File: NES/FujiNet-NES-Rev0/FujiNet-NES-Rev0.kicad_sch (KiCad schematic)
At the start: 0 parts

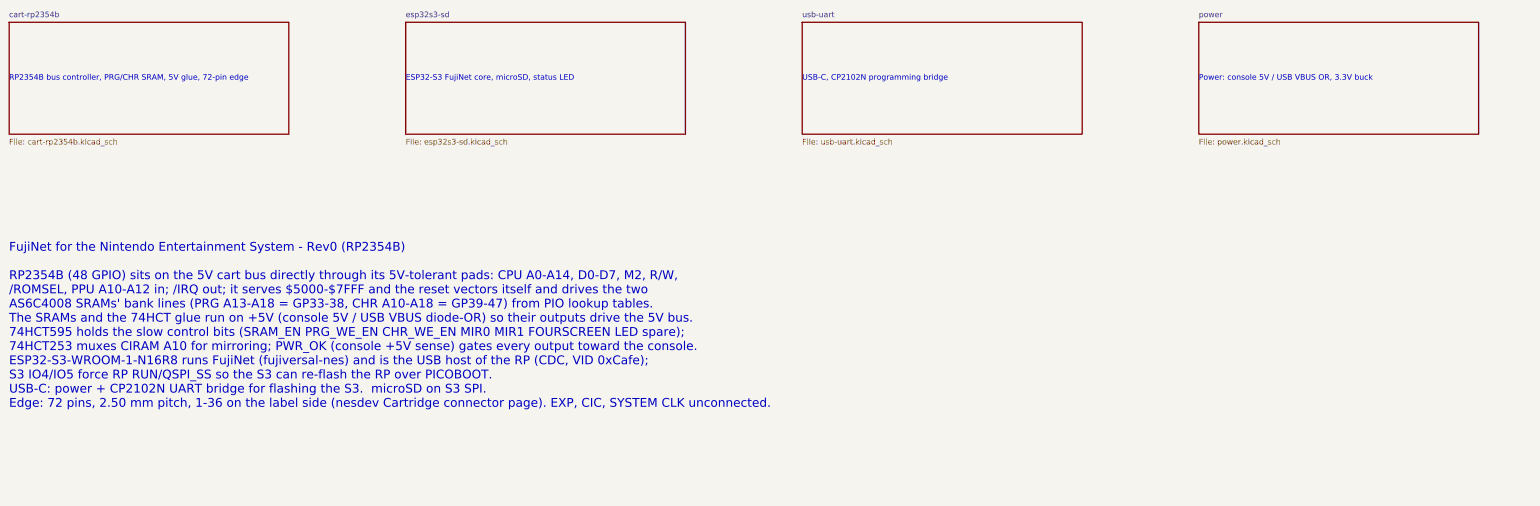
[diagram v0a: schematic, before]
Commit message: NES Rev0: audit the schematic with kicad-happy and redo it
Datasheet-backed review of the first Rev0 schematic (kicad-happy analyzer,
ngspice, 28 deep-review findings all evidence-gated, 453 netlist checks
against fujinet-firmware nes-bringup) and the fixes it called for:

- edge footprint was mirrored (pin 1 west); nesdev and two measured
  NES-EWROM-01 references put pin 1 east on the label side. Fingers are now
  2.0 x 12 mm (ends 3.0 at +/-44.25), 2.50 pitch, copper 1.0-13.0 mm in,
  Nintendo's front/back mask depths
- RP2350 pads are 5 V-tolerant only while IOVDD is powered: the IOVDD group
  moves to an AP2112K (20 us) rail +3V3_RP; VREG_VIN stays on the buck
- 74HCT595 /OE = NAND(PWR_OK, POR) with 100k pull-downs on every bit, so
  the register cannot enable the SRAMs before the RP loads it or while
  the console is off
- PRG /WE = NAND4(M2, ROMSEL, !R/W, PRG_WE_EN) on a CD74HCT20, one gate
  after M2 (was three after the console's /ROMSEL decoder vs ~30 ns hold)
- CIRAM /CE through the 74HCT253's second half, tri-stated by PWR_OK_N
- console 5 V through an AO3401A P-FET (gate = VBUS) instead of a Schottky
- console-sense divider 22k/100k (TI 74HCT14 VT+ reaches 0.70 x VCC)
- WS2812B-2020 on +5V (datasheet VDD 3.7-5.3 V, VIH 2.7 V)
- VBUS decoupling at the USB-C; CIClone (ATtiny13A, DNP) on the CIC pins

tools: design.py is the source of truth as before; check_nets.py verifies
the new decode gate by gate and asserts the edge orientation from the
footprint file; make_fp_extra.py adds SOT-23-5 / SOIC-8; export.py flags
DNP; .kicad-happy.json documents the analyzer suppressions;
docs/design-review-rev0.md is the review; tools/audit/ holds the
computations the review cites.

Co-Authored-By: Claude Fable 5.1 <noreply@anthropic.com>
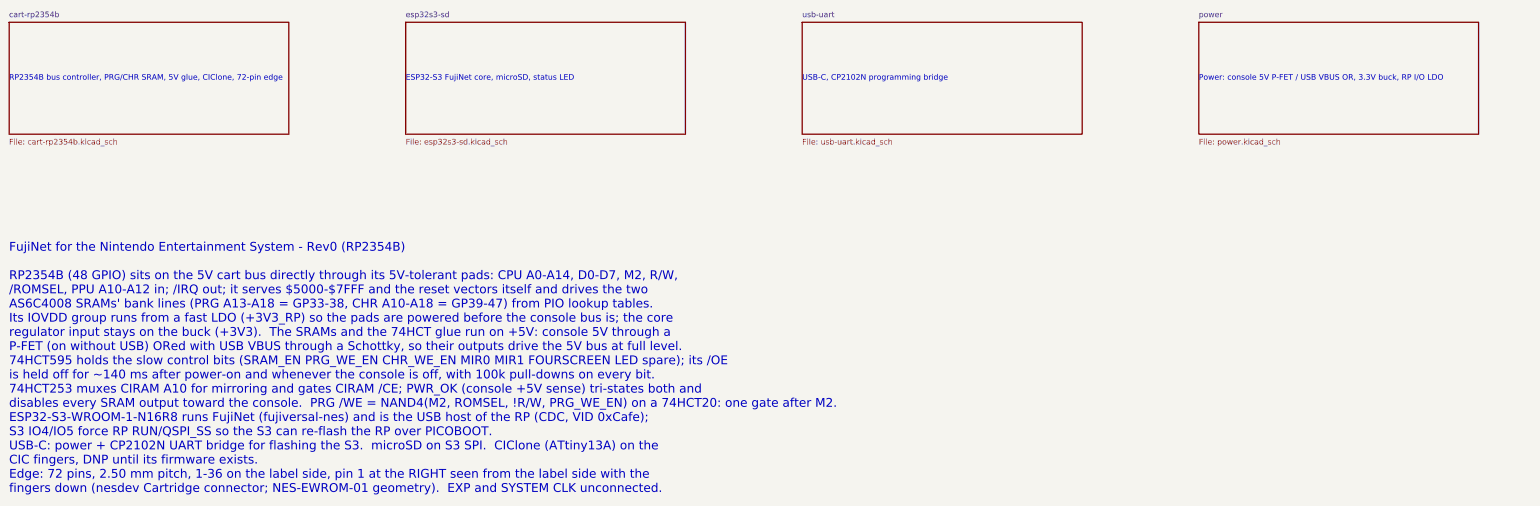
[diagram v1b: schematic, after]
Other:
- note added: "FujiNet for the Nintendo Entertainment System - Rev0 (RP2354B) RP2354B (48 GPIO) sits on the 5V cart bus directly through its 5V-tolerant pads: CPU A0-A14, D0-D7, M2, R/W, /ROMSEL, PPU A10-A12 in; /IRQ out; it serves $5000-$7FFF and the reset vectors itself and drives the two AS6C4008 SRAMs' bank lines (PRG A13-A18 = GP33-38, CHR A10-A18 = GP39-47) from PIO lookup tables. Its IOVDD group runs fro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"
- note added: "Power: console 5V P-FET / USB VBUS OR, 3.3V buck, RP I/O LDO"
- note added: "RP2354B bus controller, PRG/CHR SRAM, 5V glue, CIClone, 72-pin edge"
- note removed: "FujiNet for the Nintendo Entertainment System - Rev0 (RP2354B) RP2354B (48 GPIO) sits on the 5V cart bus directly through its 5V-tolerant pads: CPU A0-A14, D0-D7, M2, R/W, /ROMSEL, PPU A10-A12 in; /IRQ out; it serves $5000-$7FFF and the reset vectors itself and drives the two AS6C4008 SRAMs' bank lines (PRG A13-A18 = GP33-38, CHR A10-A18 = GP39-47) from PIO lookup tables. The SRAMs and the 74HCT 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"
- note removed: "Power: console 5V / USB VBUS OR, 3.3V buck"
- note removed: "RP2354B bus controller, PRG/CHR SRAM, 5V glue, 72-pin edge"
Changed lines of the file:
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@@
 	(title_block
 		(title "FujiNet NES Rev0")
-		(date "2026-09-30")
+		(date "2026-10-01")
 		(rev "0")
 		(company "FujiNet")
@@
 		)
 	)
-	(text "RP2354B bus controller, PRG/CHR SRAM, 5V glue, 72-pin edge"
+	(text "RP2354B bus controller, PRG/CHR SRAM, 5V glue, CIClone, 72-pin edge"
 		(exclude_from_sim no)
 		(at 30 52.7 0)
@@
 		)
 	)
-	(text "Power: console 5V / USB VBUS OR, 3.3V buck"
+	(text "Power: console 5V P-FET / USB VBUS OR, 3.3V buck, RP I/O LDO"
 		(exclude_from_sim no)
 		(at 300 52.7 0)
@@
 		)
 	)
-	(text "FujiNet for the Nintendo Entertainment System - Rev0 (RP2354B)\n\nRP2354B (48 GPIO) sits on the 5V cart bus directly through its 5V-tolerant pads: CPU A0-A14, D0-D7, M2, R/W,\n/ROMSEL, PPU A10-A12 in; /IRQ out; it serves $5000-$7FFF and the reset vectors itself and drives the two\nAS6C4008 SRAMs' bank lines (PRG A13-A18 = GP33-38, CHR A10-A18 = GP39-47) from PIO lookup tables.\nThe SRAMs and the 74HCT glue run on +5V (console 5V / USB VBUS diode-OR) so their outputs drive the 5V bus.\n74HCT595 holds the slow control bits (SRAM_EN PRG_WE_EN CHR_WE_EN MIR0 MIR1 FOURSCREEN LED spare);\n74HCT253 muxes CIRAM A10 for mirroring; PWR_OK (console +5V sense) gates every output toward the console.\nESP32-S3-WROOM-1-N16R8 runs FujiNet (fujiversal-nes) and is the USB host of the RP (CDC, VID 0xCafe);\nS3 IO4/IO5 force RP RUN/QSPI_SS so the S3 can re-flash the RP over PICOBOOT.\nUSB-C: power + CP2102N UART bridge for flashing the S3.  microSD on S3 SPI.\nEdge: 72 pins, 2.50 mm pitch, 1-36 on the label side (nesdev Cartridge connector page). EXP, CIC, SYSTEM CLK unconnected."
+	(text "FujiNet for the Nintendo Entertainment System - Rev0 (RP2354B)\n\nRP2354B (48 GPIO) sits on the 5V cart bus directly through its 5V-tolerant pads: CPU A0-A14, D0-D7, M2, R/W,\n/ROMSEL, PPU A10-A12 in; /IRQ out; it serves $5000-$7FFF and the reset vectors itself and drives the two\nAS6C4008 SRAMs' bank lines (PRG A13-A18 = GP33-38, CHR A10-A18 = GP39-47) from PIO lookup tables.\nIts IOVDD group runs from a fast LDO (+3V3_RP) so the pads are powered before the console bus is; the core\nregulator input stays on the buck (+3V3).  The SRAMs and the 74HCT glue run on +5V: console 5V through a\nP-FET (on without USB) ORed with USB VBUS through a Schottky, so their outputs drive the 5V bus at full level.\n74HCT595 holds the slow control bits (SRAM_EN PRG_WE_EN CHR_WE_EN MIR0 MIR1 FOURSCREEN LED spare); its /OE\nis held off for ~140 ms after power-on and whenever the console is off, with 100k pull-downs on every bit.\n74HCT253 muxes CIRAM A10 for mirroring and gates CIRAM /CE; PWR_OK (console +5V sense) tri-states both and\ndisables every SRAM output toward the console.  PRG /WE = NAND4(M2, ROMSEL, !R/W, PRG_WE_EN) on a 74HCT20: one gate after M2.\nESP32-S3-WROOM-1-N16R8 runs FujiNet (fujiversal-nes) and is the USB host of the RP (CDC, VID 0xCafe);\nS3 IO4/IO5 force RP RUN/QSPI_SS so the S3 can re-flash the RP over PICOBOOT.\nUSB-C: power + CP2102N UART bridge for flashing the S3.  microSD on S3 SPI.  CIClone (ATtiny13A) on the\nCIC fingers, DNP until its firmware exists.\nEdge: 72 pins, 2.50 mm pitch, 1-36 on the label side, pin 1 at the RIGHT seen from the label side with the\nfingers down (nesdev Cartridge connector; NES-EWROM-01 geometry).  EXP and SYSTEM CLK unconnected."
 		(exclude_from_sim no)
 		(at 30 90 0)
